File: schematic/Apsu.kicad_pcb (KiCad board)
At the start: 2 copper layers, 80 x 80 mm, 60 parts, among them J1 Conn_02x03_Odd_Even, J10 Conn_01x04_Male, J11 Conn_01x04_Male, J12 Conn_01x03, J13 Conn_01x02, J14 Conn_01x03_Female, J15 Conn_01x03, J16 Conn_01x03, J17 Conn_01x03, J18 Conn_01x02_Male, J19 Conn_01x02, J2 Conn_02x05_Odd_Even, J3 Conn_02x05_Odd_Even, J4 Conn_01x02, J5 Conn_01x02, J6 Conn_01x02, J7 Conn_01x02, J8 Conn_01x04_Male, J9 Conn_01x08_Male, SW1 SW_DIP_x01, U1 ESP32-WROOM-32, U2 LM2595S-3.3, U3 PCA9685PW, U4 MAX11613, U5 MAX485E

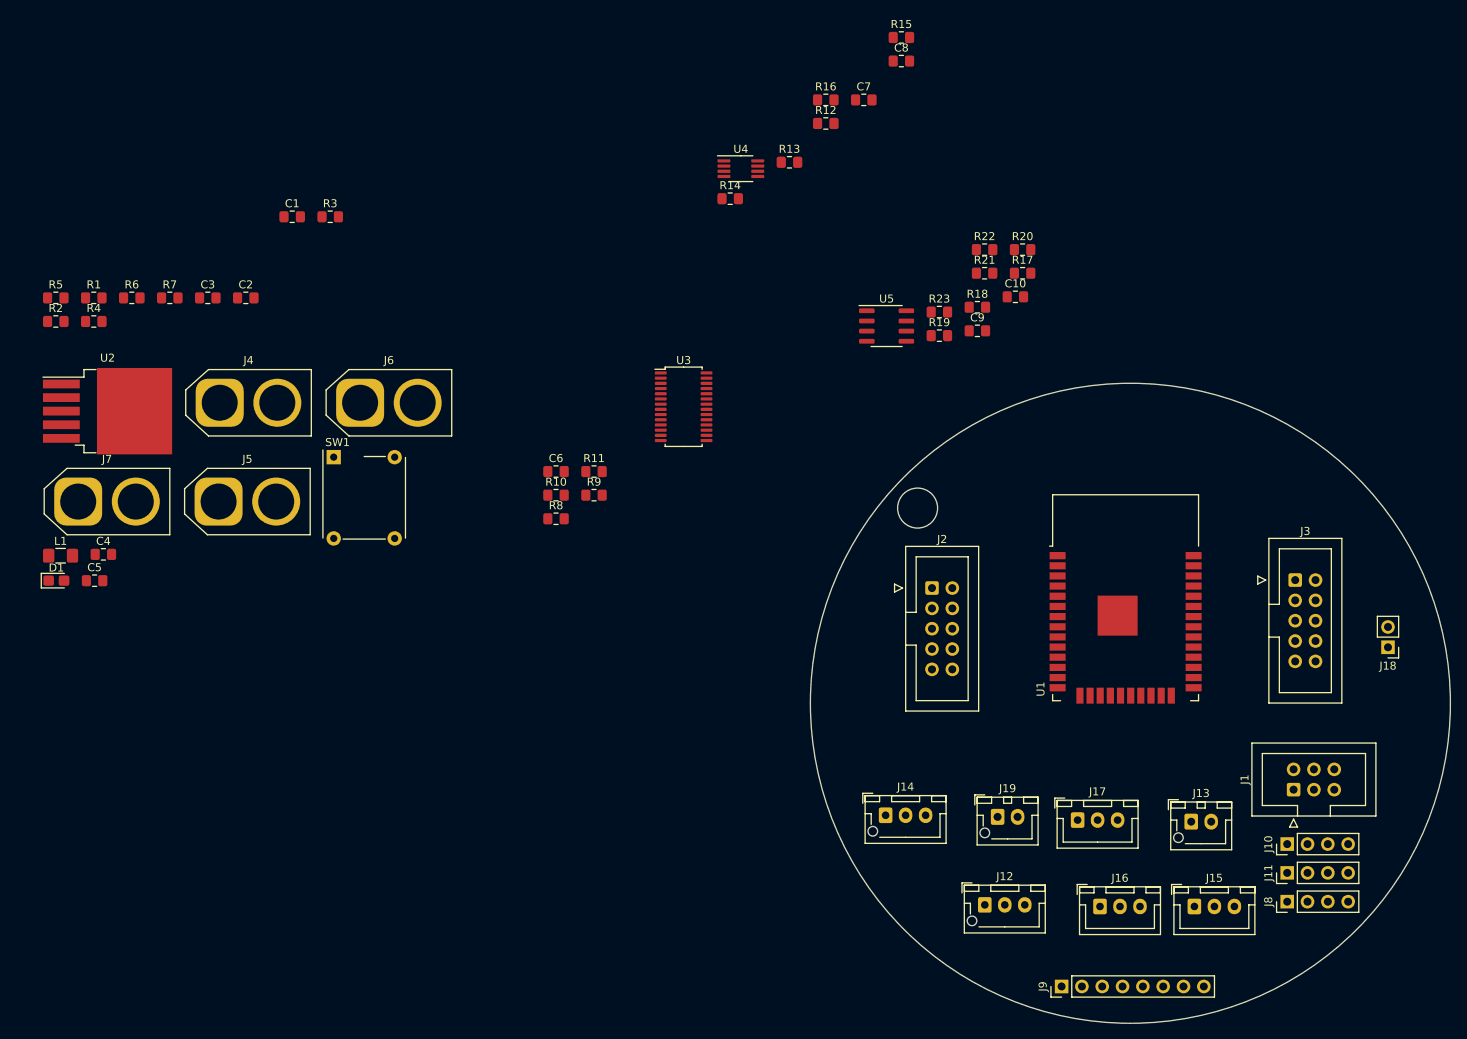
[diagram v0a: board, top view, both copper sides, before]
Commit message: added LSM6DSOX and LIS2MDL for IMU
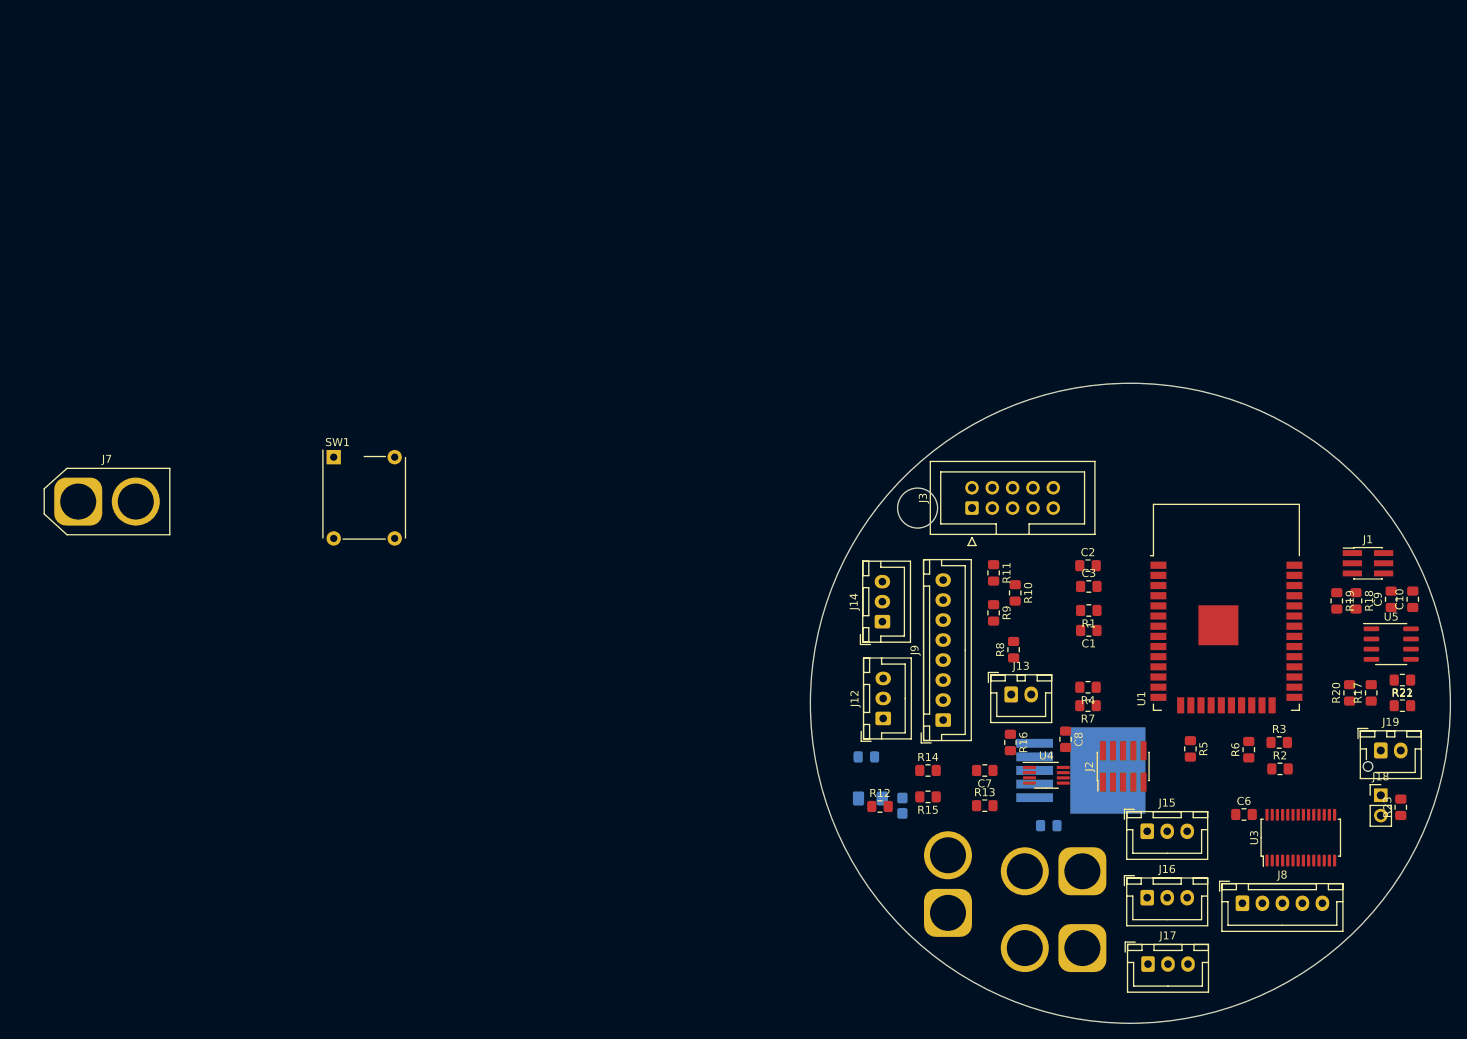
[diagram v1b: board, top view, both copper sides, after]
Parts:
- removed J10, J11: Conn_01x04_Male, Connector_PinHeader_2.54mm:PinHeader_1x04_P2.54mm_Vertical
- C4, C5, D1, J4, J5, J6, L1, U2: moved to B.Cu
- J1: footprint Connector_IDC:IDC-Header_2x03_P2.54mm_Vertical -> Connector_PinHeader_1.27mm:PinHeader_2x03_P1.27mm_Vertical_SMD
- J12, J14: footprint Connector_JST:JST_XH_B3B-XH-AM_1x03_P2.50mm_Vertical -> Connector_JST:JST_XH_B3B-XH-A_1x03_P2.50mm_Vertical
- J13: footprint Connector_JST:JST_XH_B2B-XH-AM_1x02_P2.50mm_Vertical -> Connector_JST:JST_XH_B2B-XH-A_1x02_P2.50mm_Vertical
- J2: footprint Connector_IDC:IDC-Header_2x05_P2.54mm_Vertical -> Connector_PinHeader_1.27mm:PinHeader_2x05_P1.27mm_Vertical_SMD
- J8: value Conn_01x04_Male -> Conn_01x05; footprint Connector_PinHeader_2.54mm:PinHeader_1x04_P2.54mm_Vertical -> Connector_JST:JST_XH_B5B-XH-A_1x05_P2.50mm_Vertical
- J9: footprint Connector_PinHeader_2.54mm:PinHeader_1x08_P2.54mm_Vertical -> Connector_JST:JST_XH_B8B-XH-A_1x08_P2.50mm_Vertical
- moved R2 162.9 mm to (177.7, 118.0)
- moved R5 152.6 mm to (166.5, 115.5), turned to 270 degrees
- moved R6 150.6 mm to (173.8, 115.6), turned to 90 degrees
- moved R3 135.6 mm to (177.6, 114.7)
- moved R4 132.4 mm to (153.7, 107.8), turned to 180 degrees
- moved R1 130.4 mm to (153.8, 98.2), turned to 180 degrees
- moved U2 129.7 mm to (152.8, 118.2)
- moved J4 127.6 mm to (153.0, 140.4), turned to 180 degrees
- moved R7 125.6 mm to (153.7, 110.1), turned to 180 degrees
- moved C4 122.9 mm to (148.8, 125.1)
- moved J5 117.4 mm to (153.0, 130.8), turned to 180 degrees
- moved C3 115.9 mm to (153.8, 95.2)
- moved C1 112.2 mm to (153.8, 100.7), turned to 180 degrees
- moved C2 110.5 mm to (153.7, 92.6)
- moved D1 109.4 mm to (130.5, 122.6), turned to 270 degrees
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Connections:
- J8 pad 1: BLDC_top_left -> BLDC_bottom_right
- J8 pad 2: BLDC_top_right -> BLDC_bottom_left
- J8 pad 3: BLDC_bottom_left -> BLDC_top_right
- J8 pad 4: BLDC_bottom_right -> BLDC_top_left

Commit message: new pcb design
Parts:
- added C11: 220nF, Capacitor_SMD:C_0805_2012Metric_Pad1.15x1.40mm_HandSolder, F.Cu at (165.0, 123.0)
- added C12: 100nF, Capacitor_SMD:C_0805_2012Metric_Pad1.15x1.40mm_HandSolder, F.Cu at (165.0, 125.0)
- added C13: 100nF, Capacitor_SMD:C_0805_2012Metric_Pad1.15x1.40mm_HandSolder, F.Cu at (159.5, 127.5)
- added C14: 10uF, Capacitor_SMD:C_0805_2012Metric_Pad1.15x1.40mm_HandSolder, F.Cu at (165.0, 127.0)
- added C15: 100nF, Capacitor_SMD:C_0805_2012Metric_Pad1.15x1.40mm_HandSolder, F.Cu at (172.5, 123.0)
- added C16: 100nF, Capacitor_SMD:C_0805_2012Metric_Pad1.15x1.40mm_HandSolder, F.Cu at (161.5, 124.0)
- added C17: 100nF, Capacitor_SMD:C_0805_2012Metric_Pad1.15x1.40mm_HandSolder, F.Cu at (144.0, 127.5)
- added C18: 100nF, Capacitor_SMD:C_0805_2012Metric_Pad1.15x1.40mm_HandSolder, F.Cu at (146.5, 127.5)
- added U6: LIS2MDL, Package_LGA:LGA-12_2x2mm_P0.5mm, F.Cu at (169.0, 123.5)
- added U7: LSM6DSOX, Package_LGA:LGA-14_3x2.5mm_P0.5mm_LayoutBorder3x4y, F.Cu at (158.0, 124.0)
- added U8: BME280, Package_LGA:Bosch_LGA-8_2.5x2.5mm_P0.65mm_ClockwisePinNumbering, F.Cu at (145.5, 123.5)
- C4, C5, D1, J4, J5, J6, L1, U2: moved to F.Cu
- J19: footprint Connector_JST:JST_XH_B2B-XH-AM_1x02_P2.50mm_Vertical -> Connector_JST:JST_XH_B2B-XH-A_1x02_P2.50mm_Vertical
- J9: value Conn_01x08_Male -> Conn_01x05; footprint Connector_JST:JST_XH_B8B-XH-A_1x08_P2.50mm_Vertical -> Connector_JST:JST_XH_B5B-XH-A_1x05_P2.50mm_Vertical
- moved J4 145.2 mm to (24.4, 73.1), turned to 0 degrees
- moved U2 136.9 mm to (28.0, 61.8)
- moved J5 131.2 mm to (42.1, 60.8), turned to 0 degrees
- moved C4 129.5 mm to (27.5, 79.7)
- moved D1 115.8 mm to (21.6, 83.0), turned to 0 degrees
- moved J6 113.3 mm to (41.9, 73.1), turned to 0 degrees
- moved L1 112.4 mm to (22.2, 79.9), turned to 0 degrees
- moved C5 105.1 mm to (26.4, 83.0)
- moved J8 55.9 mm to (124.0, 108.0)
- moved R12 55.6 mm to (181.5, 108.5), turned to 90 degrees
- moved R13 45.4 mm to (184.0, 108.5), turned to 270 degrees
- moved U3 44.9 mm to (136.0, 119.0), turned to 270 degrees
- moved J7 40.0 mm to (59.6, 60.8)
- moved R16 38.6 mm to (182.5, 112.0), turned to 0 degrees
- moved R17 34.8 mm to (166.0, 82.5), turned to 0 degrees
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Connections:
- J9 pad 1: Net-(J9-Pad1) -> BLDC_right_z
- J9 pad 2: Net-(J9-Pad2) -> BLDC_M4
- J9 pad 3: GND -> BLDC_left_z
- J9 pad 4: Net-(J9-Pad4) -> BLDC_M3
- J9 pad 5: BLDC_M3 -> GND
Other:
- board size 80 x 80 mm -> 76.7 x 52.7 mm

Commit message: power on seperate board
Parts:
- removed C4: C680uF, Capacitor_SMD:C_0805_2012Metric_Pad1.15x1.40mm_HandSolder
- removed C5: C220uF, Capacitor_SMD:C_0805_2012Metric_Pad1.15x1.40mm_HandSolder
- removed D1: D, Diode_SMD:D_0805_2012Metric_Castellated
- removed J3: Conn_02x05_Odd_Even, Connector_IDC:IDC-Header_2x05_P2.54mm_Vertical
- removed J4: Conn_01x02, Connector_AMASS:AMASS_XT60-M_1x02_P7.20mm_Vertical
- removed J5, J6, J7: Conn_01x02, Connector_AMASS:AMASS_XT60-F_1x02_P7.20mm_Vertical
- removed L1: L33uH, Inductor_SMD:L_1206_3216Metric_Pad1.42x1.75mm_HandSolder
- removed SW1: SW_DIP_x01, Button_Switch_THT:SW_MEC_5GTH9
- removed U5: MAX485E, Package_SO:SOIC-8_3.9x4.9mm_P1.27mm
- U2: value LM2595S-3.3 -> SP3485CN; footprint Package_TO_SOT_SMD:TO-263-5_TabPin3 -> Package_SO:SOIC-8_3.9x4.9mm_P1.27mm
- moved U2 149.9 mm to (174.5, 94.0)
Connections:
- net Net-(U1-Pad10) renamed SPI-SS1
- net Net-(U1-Pad11) renamed SPI-SS2
- net Net-(U1-Pad33) renamed SPI-SS0
- J18 pad 1: RS485-B -> RS485-A
- J19 pad 1: RS485-B -> RS485-A
- J19 pad 2: RS485-A -> RS485-B
- R10 pad 1: +3V3 -> GND
- R11 pad 1: +3V3 -> GND
- R21 pad 2: RS485-B -> RS485-A
- R22 pad 1: RS485-A -> RS485-B
- R23 pad 2: RS485-A -> RS485-B
- R8 pad 1: +3V3 -> GND
- R9 pad 1: +3V3 -> GND
- U1 pad 24: SPI-UART_SS -> Net-(U1-Pad24)
- U2 pad 1: Net-(D1-Pad1) -> RS485-RX
- U2 pad 2: +12V -> RS485-RTS
- U2 pad 3: GND -> RS485-RTS
- U2 pad 4: +3V3 -> RS485-TX

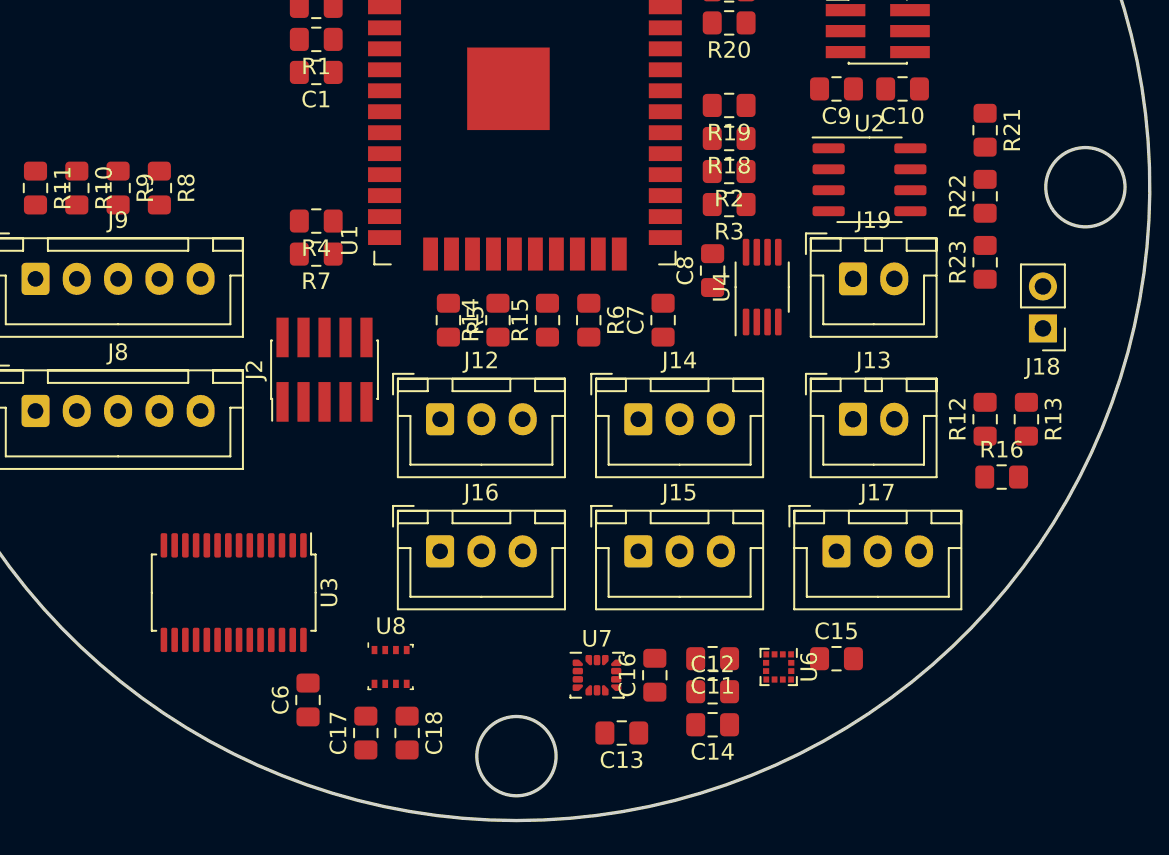
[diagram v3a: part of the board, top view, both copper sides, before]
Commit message: boost converter on Apsu board and PCB design
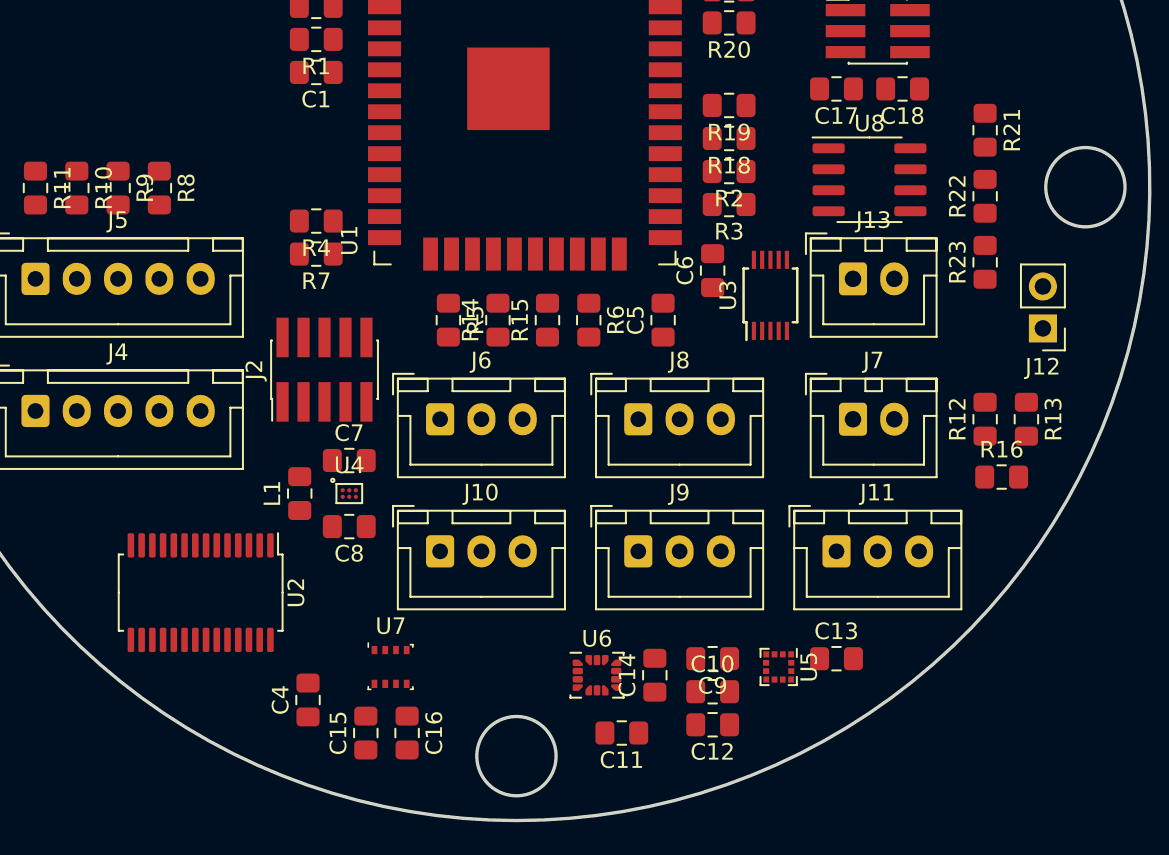
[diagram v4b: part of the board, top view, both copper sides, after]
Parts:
- added C7: 2.2uF, Capacitor_SMD:C_0805_2012Metric_Pad1.15x1.40mm_HandSolder, F.Cu at (143.0, 111.0)
- added C8: 4.7uF, Capacitor_SMD:C_0805_2012Metric_Pad1.15x1.40mm_HandSolder, F.Cu at (143.0, 115.0)
- added L1: 1uH, Inductor_SMD:L_0805_2012Metric_Pad1.15x1.40mm_HandSolder, F.Cu at (140.0, 113.0)
- added U3: ADS1015IDGS, Package_SO:TSSOP-10_3x3mm_P0.5mm, F.Cu at (168.5, 101.0)
- U4: value MAX11613 -> FAN4860UC5X; footprint Package_SO:MSOP-8_3x3mm_P0.65mm -> Package_CSP:WLCSP-6_1.4x1.0mm_P0.4mm
- moved U4 28.0 mm to (143.0, 113.0), turned to 0 degrees
- moved U2 2.00 mm to (134.0, 119.0)
- renumbered C12 to C10, C13 to C11, C14 to C12, C15 to C13, C16 to C14, C17 to C15, C18 to C16, C9 to C17, C10 to C18, C6 to C4, C7 to C5, C8 to C6, C11 to C9, J16 to J10, J17 to J11, J18 to J12, J19 to J13, J8 to J4, J9 to J5, J12 to J6, J13 to J7, J14 to J8, J15 to J9, U3 to U2, U6 to U5, U7 to U6, U8 to U7, U2 to U8

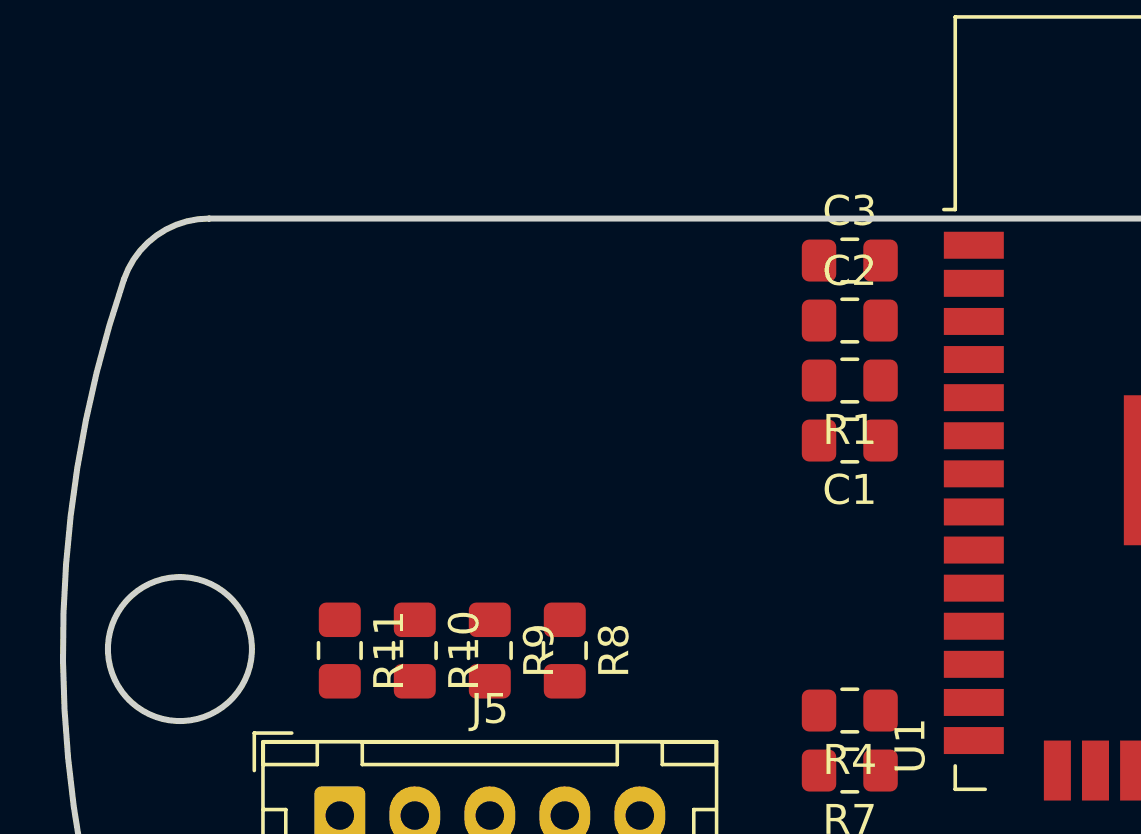
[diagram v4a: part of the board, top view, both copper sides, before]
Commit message: added 14pin header
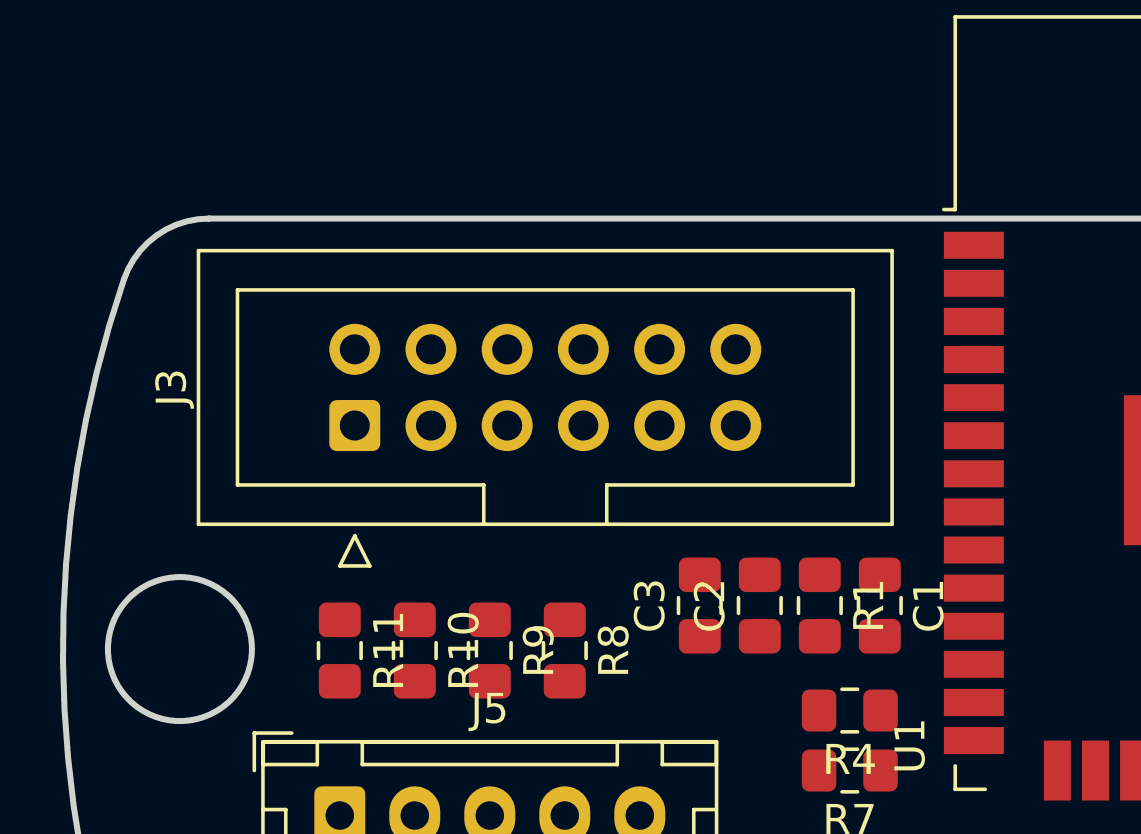
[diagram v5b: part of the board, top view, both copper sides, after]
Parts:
- added J3: Conn_02x06_Odd_Even, Connector_IDC:IDC-Header_2x06_P2.54mm_Vertical, F.Cu at (124.5, 87.0)
- moved C3 12.5 mm to (136.0, 93.0), turned to 90 degrees
- moved C2 9.96 mm to (138.0, 93.0), turned to 90 degrees
- moved R1 7.57 mm to (140.0, 93.0), turned to 270 degrees
- moved C1 5.59 mm to (142.0, 93.0), turned to 270 degrees
